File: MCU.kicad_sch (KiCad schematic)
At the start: 18 parts, among them U3 ESP32-C6-MINI-1

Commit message: Added eframe circuit: - Must replace 10uF caps with higher voltage rated ones - Should double check all the wiring - Assign MCU GPIOs now that all peripherals have their pins assigned
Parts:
- renumbered C6 to C20, C7 to C21, C8 to C22, C9 to C23, R9 to R19, R10 to R20, R11 to R21, R12 to R22, R13 to R23, R14 to R24, R15 to R25, R16 to R26, R17 to R27, R18 to R28, R19 to R29, U3 to U4

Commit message: Final touches on schematic: Added test points Added LED Fixed symbol footprints
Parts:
- removed R20, R21, R22, R24, R25, R26, R28, R29: 10kΩ, PCM_JLCPCB:R_0402, symbol PCM_JLCPCB-Resistors:0402,10kΩ
- added TP14, TP15, TP16, TP17, TP18: TestPoint_EPD_RST, TestPoint:TestPoint_Pad_D1.5mm, symbol Connector:TestPoint_Probe
- renumbered C20 to C22, C21 to C23, C22 to C24, C23 to C25, R19 to R21, R23 to R22, R27 to R23, S1 to S3, S2 to S4, U4 to U2
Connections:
- net CS0(EPD): now also TP17.1
- net CS1(SD): now also U2.25 (IO19), TP18.1; no longer U2.13 (IO1)
- net SPI2.MISO: now also TP15.1
- net SPI2.MOSI: now also TP14.1
- net SPI2.SCK: now also TP16.1
- net GPIO14: now reaches U2.19 (IO14)
- net GPIO15: now reaches U2.20 (IO15)
- net GPIO18: now reaches U2.24 (IO18)
- net GPIO20: now reaches U2.26 (IO20)
- net GPIO21: now reaches U2.27 (IO21)
- net GPIO22: now reaches U2.28 (IO22)
- net GPIO23: now reaches U2.29 (IO23)
- net GPIO18(RTX): now reaches U2.30 (RXD0)
- net GPIO17(RX): now reaches U2.31 (TXD0)
- net GPIO3: now reaches U2.6 (IO3)
- new net GPIO1: U2.13 (IO1)
- no-connect marks 2 -> 4
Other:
- note added: "3V3 power plane"
- note added: "5V also power plane"
- note added: "Available during Low Power"
- note added: "BOOT/RST"
- note added: "Buttons/Switch"
- note added: "D+-"
- note added: "EPD driver"
- note added: "Global power circuit"
- note added: "IO"
- note added: "In Software: - Set pins to high-Z before deep sleep There may be leakage current on SPI even with power gating of VCC - Use internal pullups when ON"
- note added: "LiPo"
- note added: "MCU"
- note added: "PCU"
- note added: "RGB LED"
- note added: "SD card"
- note added: "SD_DETECT"
- note added: "Test points"
- note added: "USB"
- moved on the sheet: C23, C24, C25, U2

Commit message: Schematic cleanup and initial layout complete
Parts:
- C26: renamed from C25; footprint PCM_JLCPCB:C_0603 -> PCM_JLCPCB:C_0402; symbol PCM_JLCPCB-Capacitors:0603,100nF -> PCM_JLCPCB-Capacitors:0402,100nF,(2); LCSC C14663 -> C307331; Manufacturer YAGEO -> Samsung Electro-Mechanics; Part CC0603KRX7R9BB104 -> CL05B104KB54PNC; Price 0.006USD -> 0.008USD; Stock 70324515 -> 8389599
- TP14: renamed from TP18; value TestPoint_EPD_RST -> TestPoint_CS1
- TP15: renamed from TP17; value TestPoint_EPD_RST -> TestPoint_CS0
- TP16: renamed from TP14; value TestPoint_EPD_RST -> TestPoint_MOSI
- TP17: renamed from TP15; value TestPoint_EPD_RST -> TestPoint_MISO
- TP18: renamed from TP16; value TestPoint_EPD_RST -> TestPoint_SCK
- renumbered C22 to C23, C23 to C24, C24 to C25, R21 to R24, R22 to R25, R23 to R26, U2 to U3
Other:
- company: (none) -> Josef
- title: (none) -> MCU interface

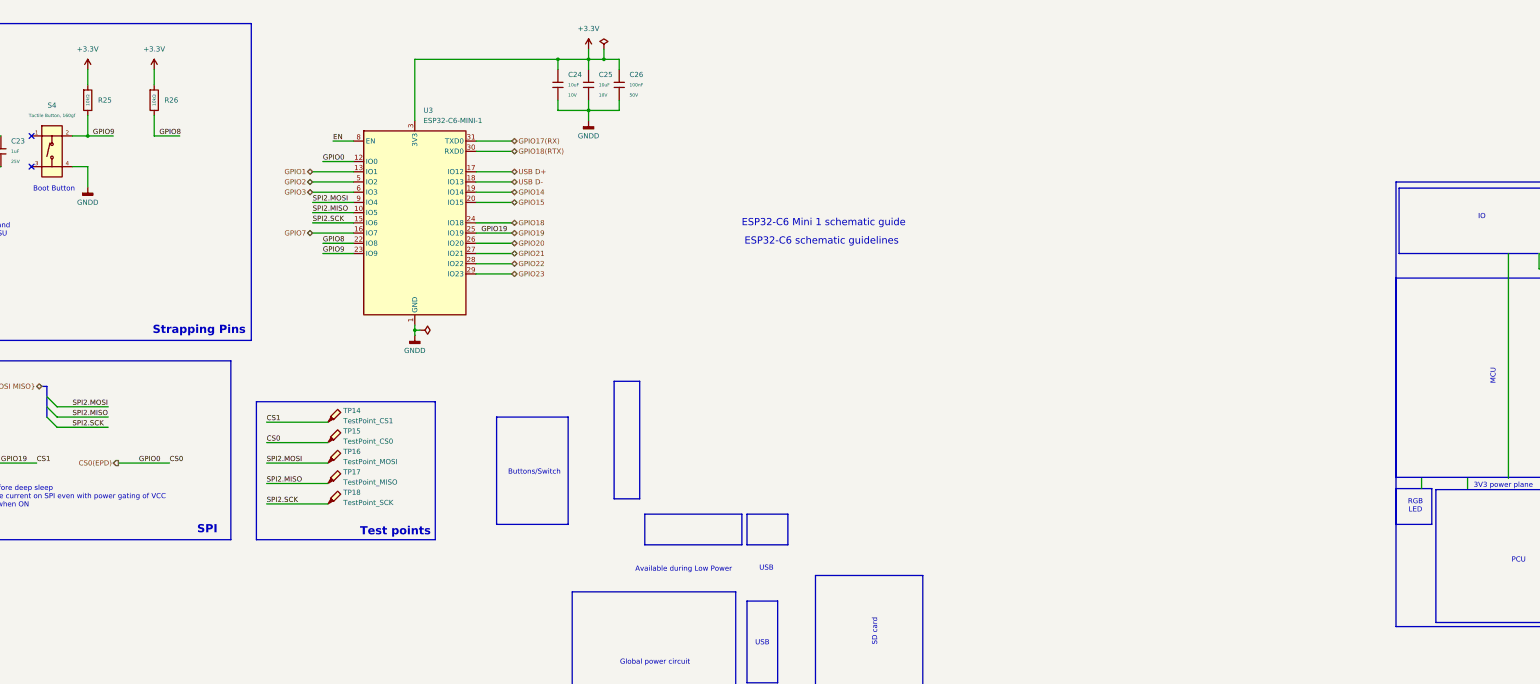
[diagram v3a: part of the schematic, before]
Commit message: Changed some parts for more common ones
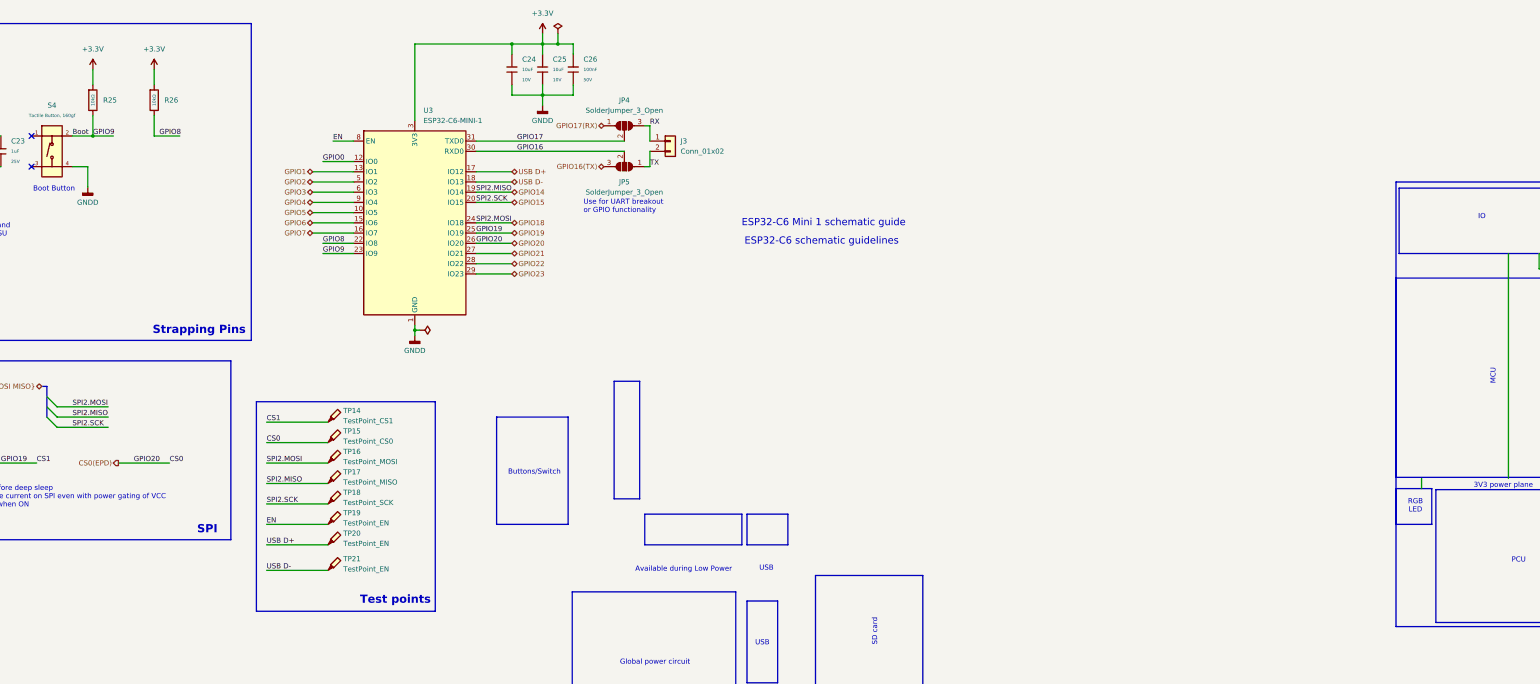
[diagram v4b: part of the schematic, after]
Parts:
- added J3: Conn_01x02, Connector_PinHeader_2.54mm:PinHeader_1x02_P2.54mm_Vertical, symbol Connector_Generic:Conn_01x02
- added JP4, JP5: SolderJumper_3_Open, Jumper:SolderJumper-3_P1.3mm_Open_RoundedPad1.0x1.5mm, symbol Jumper:SolderJumper_3_Open
- added TP19, TP20, TP21: TestPoint_EN, TestPoint:TestPoint_Pad_D1.5mm, symbol Connector:TestPoint_Probe
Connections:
- net GPIO20 is gone; now on net CS0(EPD): U3.26 (IO20)
- net CS0(EPD): no longer U3.12 (IO0)
- net EN: now also TP19.1
- net GPIO14: now also TP17.1
- net GPIO15: now also TP18.1
- net GPIO17(RX): now also JP4.1 (A); no longer U3.31 (TXD0)
- net GPIO18: now also TP16.1
- net USB D+: now also TP20.1
- net USB D-: now also TP21.1
- net GPIO18(RTX) renamed GPIO16
- net GPIO16: now also JP5.2 (C)
- net GPIO9 renamed Boot
- net SPI2.MISO renamed GPIO5
- net GPIO5: no longer TP17.1
- net SPI2.MOSI renamed GPIO4
- net GPIO4: no longer TP16.1
- net SPI2.SCK renamed GPIO6
- net GPIO6: no longer TP18.1
- new net GPIO0: U3.12 (IO0)
- new net GPIO16(TX): JP5.3 (B)
- new net GPIO17: JP4.2 (C), U3.31 (TXD0)
- new net RX: J3.1 (Pin_1), JP4.3 (B)
- new net TX: J3.2 (Pin_2), JP5.1 (A)
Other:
- note added: "Use for UART breakout or GPIO functionality"
- moved on the sheet: C24, C25, C26, R25

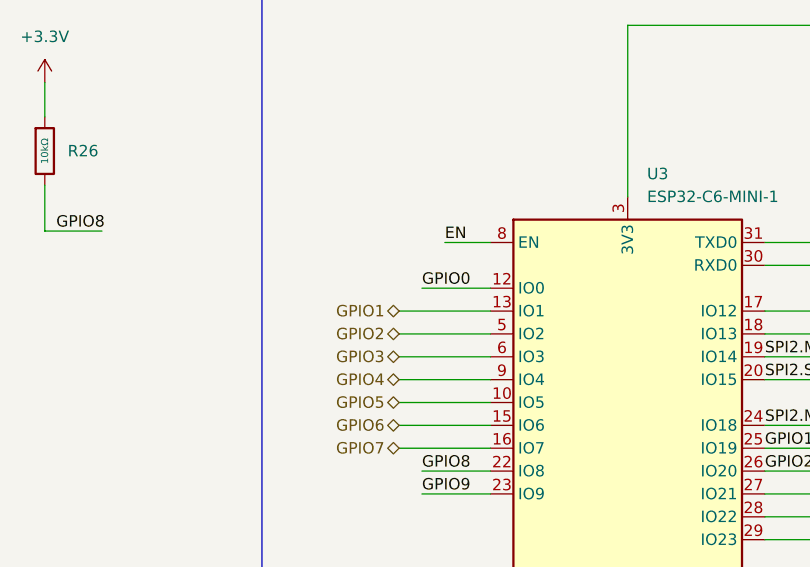
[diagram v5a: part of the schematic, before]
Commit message: First draft of layout done. Needs cleaning and DRC
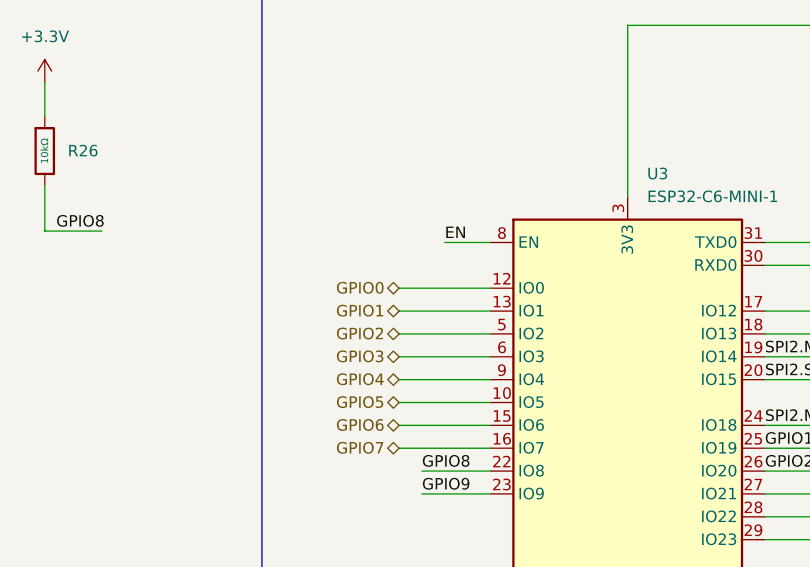
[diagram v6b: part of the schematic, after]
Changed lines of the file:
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@@
 	(wire
 		(pts
-			(xy 123.19 49.53) (xy 130.81 49.53)
-		)
-		(stroke
-			(width 0)
-			(type default)
-		)
-	)
-	(wire
-		(pts
 			(xy 57.15 113.03) (xy 69.85 113.03)
 		)
@@
 	(wire
 		(pts
+			(xy 120.65 49.53) (xy 130.81 49.53)
+		)
+		(stroke
+			(width 0)
+			(type default)
+		)
+	)
+	(wire
+		(pts
 			(xy 72.39 124.46) (xy 85.09 124.46)
 		)
@@
 		)
 	)
-	(label "GPIO0"
-		(at 123.19 49.53 0)
-		(effects
-			(font
-				(size 1.27 1.27)
-			)
-			(justify left bottom)
-		)
-	)
 	(label "GPIO20"
 		(at 161.29 69.85 0)
@@
 		)
 	)
+	(hierarchical_label "GPIO0"
+		(shape bidirectional)
+		(at 120.65 49.53 180)
+		(effects
+			(font
+				(size 1.27 1.27)
+			)
+			(justify right)
+		)
+	)
